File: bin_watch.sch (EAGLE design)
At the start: 88 parts, among them IC1 MEGA48/88/168-AU, J1 USB3100-XX-X_REVB, Q1 32.768kHz, T1 2N7002BKV, T2 2N7002BKV, T3 2N7002BKV, T4 2N7002BKV, T5 PMDT670UPE, T6 PMDT670UPE, T7 PMDT670UPE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

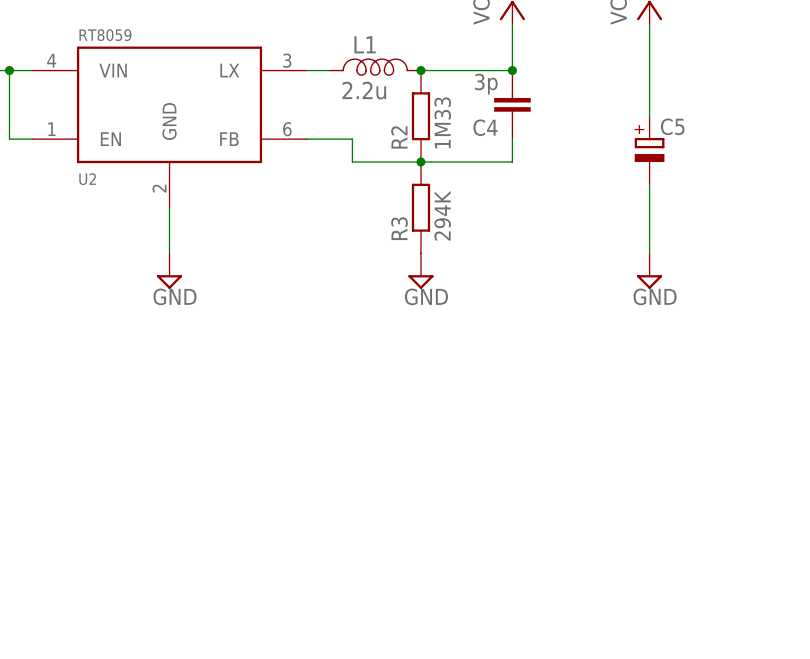
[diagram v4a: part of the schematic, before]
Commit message: Added potentiometer
This is to enable small adjustments to the system voltage around 3.5 V
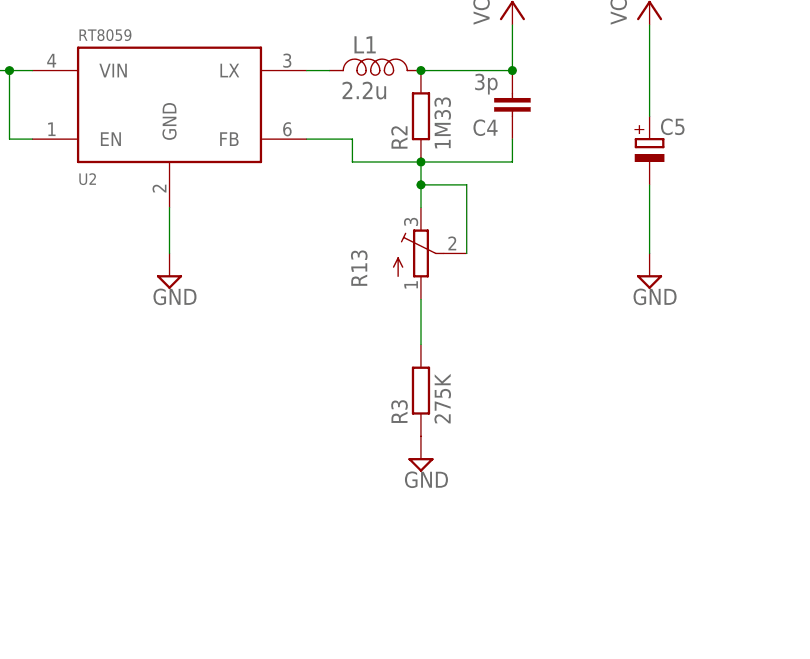
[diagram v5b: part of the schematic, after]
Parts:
- added R13: (no value), pot:TRIM_EU-3223J
- C1, C2, C3, C4: device rcl:C-EUC0805 -> rcl:C-EUC0603
- R1, R2, R4: device rcl:R-EU_R0805 -> rcl:R-EU_R0603
- R3: value 294K -> 275K; device rcl:R-EU_R0805 -> rcl:R-EU_R0603
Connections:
- new net N$10: R13.A, R3.2
- net FB: now also R13.E, R13.S; no longer R3.2
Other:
- moved on the sheet: R3
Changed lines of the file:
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@@
 <parts>
 <part name="Q1" library="crystal-geyer_V1_0" library_urn="urn:adsk.eagle:library:203" deviceset="KX-327" device="-NHF" value="32.768kHz"/>
-<part name="C1" library="rcl" library_urn="urn:adsk.eagle:library:334" deviceset="C-EU" device="C0805" package3d_urn="urn:adsk.eagle:package:23617/1" value="10pF"/>
+<part name="C1" library="rcl" library_urn="urn:adsk.eagle:library:334" deviceset="C-EU" device="C0603" package3d_urn="urn:adsk.eagle:package:23616/1" value="10pF"/>
 <part name="SUPPLY2" library="supply2" library_urn="urn:adsk.eagle:library:372" deviceset="GND" device=""/>
 <part name="JP1" library="avr-5" deviceset="AVR-ISP-6" device=""/>
@@
 <part name="SUPPLY17" library="supply2" library_urn="urn:adsk.eagle:library:372" deviceset="GND" device=""/>
 <part name="SUPPLY18" library="supply2" library_urn="urn:adsk.eagle:library:372" deviceset="GND" device=""/>
-<part name="R1" library="rcl" library_urn="urn:adsk.eagle:library:334" deviceset="R-EU_" device="R0805" package3d_urn="urn:adsk.eagle:package:23553/1" value="2K"/>
+<part name="R1" library="rcl" library_urn="urn:adsk.eagle:library:334" deviceset="R-EU_" device="R0603" package3d_urn="urn:adsk.eagle:package:23555/1" value="2K"/>
 <part name="SUPPLY19" library="supply2" library_urn="urn:adsk.eagle:library:372" deviceset="GND" device=""/>
 <part name="STAT_LED" library="standardparts" deviceset="LED" device=".0603" value="R"/>
-<part name="R4" library="rcl" library_urn="urn:adsk.eagle:library:334" deviceset="R-EU_" device="R0805" package3d_urn="urn:adsk.eagle:package:23553/1" value="470R"/>
-<part name="C3" library="rcl" library_urn="urn:adsk.eagle:library:334" deviceset="C-EU" device="C0805" package3d_urn="urn:adsk.eagle:package:23617/1" value="4.7u"/>
+<part name="R4" library="rcl" library_urn="urn:adsk.eagle:library:334" deviceset="R-EU_" device="R0603" package3d_urn="urn:adsk.eagle:package:23555/1" value="470R"/>
+<part name="C3" library="rcl" library_urn="urn:adsk.eagle:library:334" deviceset="C-EU" device="C0603" package3d_urn="urn:adsk.eagle:package:23616/1" value="4.7u"/>
 <part name="SUPPLY20" library="supply2" library_urn="urn:adsk.eagle:library:372" deviceset="GND" device=""/>
-<part name="C2" library="rcl" library_urn="urn:adsk.eagle:library:334" deviceset="C-EU" device="C0805" package3d_urn="urn:adsk.eagle:package:23617/1" value="4.7u"/>
+<part name="C2" library="rcl" library_urn="urn:adsk.eagle:library:334" deviceset="C-EU" device="C0603" package3d_urn="urn:adsk.eagle:package:23616/1" value="4.7u"/>
 <part name="SUPPLY21" library="supply2" library_urn="urn:adsk.eagle:library:372" deviceset="GND" device=""/>
 <part name="SUPPLY22" library="supply2" library_urn="urn:adsk.eagle:library:372" deviceset="GND" device=""/>
@@
 <part name="U2" library="pmg-library" deviceset="RT8059" device=""/>
 <part name="L1" library="inductor" deviceset="COIL-H" device="I" value="2.2u"/>
-<part name="R2" library="rcl" library_urn="urn:adsk.eagle:library:334" deviceset="R-EU_" device="R0805" package3d_urn="urn:adsk.eagle:package:23553/1" value="1M33"/>
-<part name="R3" library="rcl" library_urn="urn:adsk.eagle:library:334" deviceset="R-EU_" device="R0805" package3d_urn="urn:adsk.eagle:package:23553/1" value="294K"/>
-<part name="C4" library="rcl" library_urn="urn:adsk.eagle:library:334" deviceset="C-EU" device="C0805" package3d_urn="urn:adsk.eagle:package:23617/1" value="3p"/>
+<part name="R2" library="rcl" library_urn="urn:adsk.eagle:library:334" deviceset="R-EU_" device="R0603" package3d_urn="urn:adsk.eagle:package:23555/1" value="1M33"/>
+<part name="R3" library="rcl" library_urn="urn:adsk.eagle:library:334" deviceset="R-EU_" device="R0603" package3d_urn="urn:adsk.eagle:package:23555/1" value="275K"/>
+<part name="C4" library="rcl" library_urn="urn:adsk.eagle:library:334" deviceset="C-EU" device="C0603" package3d_urn="urn:adsk.eagle:package:23616/1" value="3p"/>
 <part name="SUPPLY23" library="supply2" library_urn="urn:adsk.eagle:library:372" deviceset="GND" device=""/>
 <part name="P+9" library="supply1" library_urn="urn:adsk.eagle:library:371" deviceset="VCC" device=""/>
@@
 <part name="R11" library="rcl" library_urn="urn:adsk.eagle:library:334" deviceset="R-EU_" device="R0603" package3d_urn="urn:adsk.eagle:package:23555/1" value="12"/>
 <part name="R12" library="rcl" library_urn="urn:adsk.eagle:library:334" deviceset="R-EU_" device="R0603" package3d_urn="urn:adsk.eagle:package:23555/1" value="12"/>
+<part name="R13" library="pot" library_urn="urn:adsk.eagle:library:331" deviceset="TRIM_EU-" device="3223J" package3d_urn="urn:adsk.eagle:package:22724/1"/>
 </parts>
 <sheets>
@@
 <instance part="L1" gate="G$1" x="236.22" y="246.38"/>
 <instance part="R2" gate="G$1" x="241.3" y="241.3" rot="R90"/>
-<instance part="R3" gate="G$1" x="241.3" y="231.14" rot="R90"/>
+<instance part="R3" gate="G$1" x="241.3" y="210.82" rot="R90"/>
 <instance part="C4" gate="G$1" x="251.46" y="241.3" rot="R180"/>
-<instance part="SUPPLY23" gate="GND" x="241.3" y="223.52"/>
+<instance part="SUPPLY23" gate="GND" x="241.3" y="203.2"/>
 <instance part="P+9" gate="VCC" x="266.7" y="254"/>
 <instance part="C5" gate="G$1" x="266.7" y="238.76"/>
@@
 <instance part="R11" gate="G$1" x="266.7" y="55.88"/>
 <instance part="R12" gate="G$1" x="274.32" y="53.34"/>
+<instance part="R13" gate="1" x="241.3" y="226.06"/>
 </instances>
 <busses>
@@
 <net name="FB" class="0">
 <segment>
-<pinref part="R2" gate="G$1" pin="1"/>
-<pinref part="R3" gate="G$1" pin="2"/>
 <pinref part="U2" gate="G$1" pin="FB"/>
 <wire x1="228.6" y1="238.76" x2="233.68" y2="238.76" width="0.1524" layer="91"/>
 <wire x1="233.68" y1="238.76" x2="233.68" y2="236.22" width="0.1524" layer="91"/>
+<pinref part="R2" gate="G$1" pin="1"/>
+<pinref part="R13" gate="1" pin="E"/>
+<wire x1="241.3" y1="231.14" x2="241.3" y2="233.68" width="0.1524" layer="91"/>
+<wire x1="241.3" y1="233.68" x2="241.3" y2="236.22" width="0.1524" layer="91"/>
 <wire x1="233.68" y1="236.22" x2="241.3" y2="236.22" width="0.1524" layer="91"/>
 <junction x="241.3" y="236.22"/>
 <pinref part="C4" gate="G$1" pin="1"/>
+<wire x1="251.46" y1="236.22" x2="251.46" y2="238.76" width="0.1524" layer="91"/>
 <wire x1="241.3" y1="236.22" x2="251.46" y2="236.22" width="0.1524" layer="91"/>
-<wire x1="251.46" y1="236.22" x2="251.46" y2="238.76" width="0.1524" layer="91"/>
+<pinref part="R13" gate="1" pin="S"/>
+<wire x1="246.38" y1="226.06" x2="246.38" y2="233.68" width="0.1524" layer="91"/>
+<wire x1="246.38" y1="233.68" x2="241.3" y2="233.68" width="0.1524" layer="91"/>
+<junction x="241.3" y="233.68"/>
 </segment>
 </net>
@@
 </segment>
 </net>
+<net name="N$10" class="0">
+<segment>
+<pinref part="R3" gate="G$1" pin="2"/>
+<pinref part="R13" gate="1" pin="A"/>
+<wire x1="241.3" y1="220.98" x2="241.3" y2="215.9" width="0.1524" layer="91"/>
+</segment>
+</net>

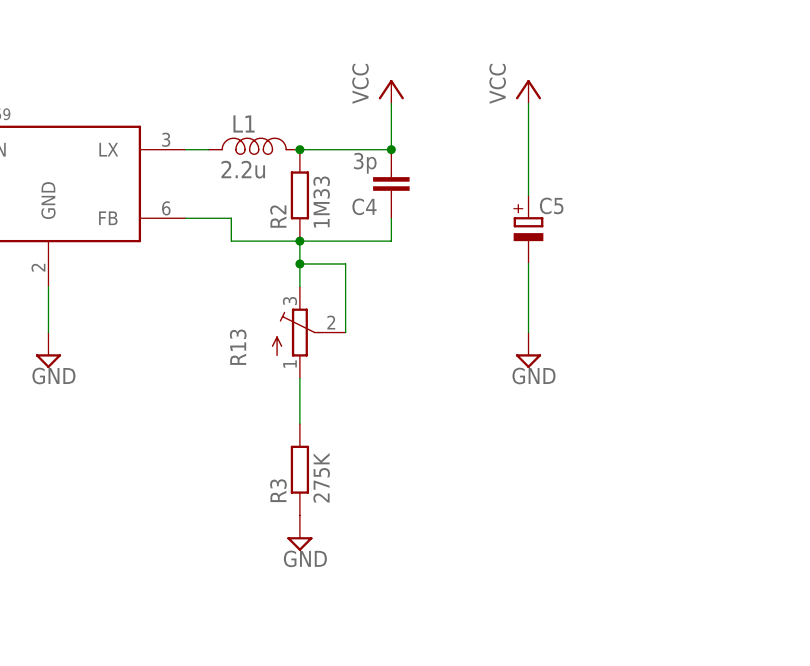
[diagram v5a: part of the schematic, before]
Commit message: Little tweaks
Ipdated component names, positions, and version label.
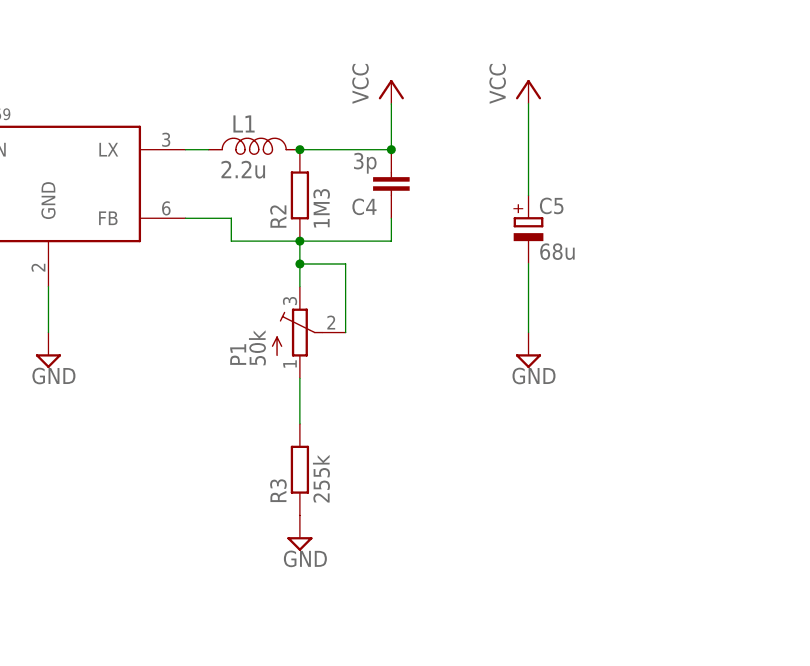
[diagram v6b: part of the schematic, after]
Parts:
- C5: value (none) -> 68u
- P1: value (none) -> 50k
- R2: value 1M33 -> 1M3
- R3: value 275K -> 255k
- renumbered R13 to P1
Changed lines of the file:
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@@
 <part name="U2" library="pmg-library" deviceset="RT8059" device=""/>
 <part name="L1" library="inductor" deviceset="COIL-H" device="I" value="2.2u"/>
-<part name="R2" library="rcl" library_urn="urn:adsk.eagle:library:334" deviceset="R-EU_" device="R0603" package3d_urn="urn:adsk.eagle:package:23555/1" value="1M33"/>
-<part name="R3" library="rcl" library_urn="urn:adsk.eagle:library:334" deviceset="R-EU_" device="R0603" package3d_urn="urn:adsk.eagle:package:23555/1" value="275K"/>
+<part name="R2" library="rcl" library_urn="urn:adsk.eagle:library:334" deviceset="R-EU_" device="R0603" package3d_urn="urn:adsk.eagle:package:23555/1" value="1M3"/>
+<part name="R3" library="rcl" library_urn="urn:adsk.eagle:library:334" deviceset="R-EU_" device="R0603" package3d_urn="urn:adsk.eagle:package:23555/1" value="255k"/>
 <part name="C4" library="rcl" library_urn="urn:adsk.eagle:library:334" deviceset="C-EU" device="C0603" package3d_urn="urn:adsk.eagle:package:23616/1" value="3p"/>
 <part name="SUPPLY23" library="supply2" library_urn="urn:adsk.eagle:library:372" deviceset="GND" device=""/>
 <part name="P+9" library="supply1" library_urn="urn:adsk.eagle:library:371" deviceset="VCC" device=""/>
-<part name="C5" library="rcl" library_urn="urn:adsk.eagle:library:334" deviceset="CPOL-EU" device="B/3528-21R" package3d_urn="urn:adsk.eagle:package:23409/1"/>
+<part name="C5" library="rcl" library_urn="urn:adsk.eagle:library:334" deviceset="CPOL-EU" device="B/3528-21R" package3d_urn="urn:adsk.eagle:package:23409/1" value="68u"/>
 <part name="R5" library="rcl" library_urn="urn:adsk.eagle:library:334" deviceset="R-EU_" device="R0603" package3d_urn="urn:adsk.eagle:package:23555/1" value="12"/>
 <part name="R6" library="rcl" library_urn="urn:adsk.eagle:library:334" deviceset="R-EU_" device="R0603" package3d_urn="urn:adsk.eagle:package:23555/1" value="12"/>
@@
 <part name="R11" library="rcl" library_urn="urn:adsk.eagle:library:334" deviceset="R-EU_" device="R0603" package3d_urn="urn:adsk.eagle:package:23555/1" value="12"/>
 <part name="R12" library="rcl" library_urn="urn:adsk.eagle:library:334" deviceset="R-EU_" device="R0603" package3d_urn="urn:adsk.eagle:package:23555/1" value="12"/>
-<part name="R13" library="pot" library_urn="urn:adsk.eagle:library:331" deviceset="TRIM_EU-" device="3223J" package3d_urn="urn:adsk.eagle:package:22724/1"/>
+<part name="P1" library="pot" library_urn="urn:adsk.eagle:library:331" deviceset="TRIM_EU-" device="3223J" package3d_urn="urn:adsk.eagle:package:22724/1" value="50k"/>
 </parts>
 <sheets>
@@
 <instance part="R11" gate="G$1" x="266.7" y="55.88"/>
 <instance part="R12" gate="G$1" x="274.32" y="53.34"/>
-<instance part="R13" gate="1" x="241.3" y="226.06"/>
+<instance part="P1" gate="1" x="241.3" y="226.06"/>
 </instances>
 <busses>
@@
 <wire x1="233.68" y1="238.76" x2="233.68" y2="236.22" width="0.1524" layer="91"/>
 <pinref part="R2" gate="G$1" pin="1"/>
-<pinref part="R13" gate="1" pin="E"/>
+<pinref part="P1" gate="1" pin="E"/>
 <wire x1="241.3" y1="231.14" x2="241.3" y2="233.68" width="0.1524" layer="91"/>
 <wire x1="241.3" y1="233.68" x2="241.3" y2="236.22" width="0.1524" layer="91"/>
@@
 <wire x1="251.46" y1="236.22" x2="251.46" y2="238.76" width="0.1524" layer="91"/>
 <wire x1="241.3" y1="236.22" x2="251.46" y2="236.22" width="0.1524" layer="91"/>
-<pinref part="R13" gate="1" pin="S"/>
+<pinref part="P1" gate="1" pin="S"/>
 <wire x1="246.38" y1="226.06" x2="246.38" y2="233.68" width="0.1524" layer="91"/>
 <wire x1="246.38" y1="233.68" x2="241.3" y2="233.68" width="0.1524" layer="91"/>
@@
 <segment>
 <pinref part="R3" gate="G$1" pin="2"/>
-<pinref part="R13" gate="1" pin="A"/>
+<pinref part="P1" gate="1" pin="A"/>
 <wire x1="241.3" y1="220.98" x2="241.3" y2="215.9" width="0.1524" layer="91"/>
 </segment>

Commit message: Added fiducial marks
Some minor adjustments to the traces, and added fiducial marks for the board and for the chip.
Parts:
- added U$1, U$2, U$3: FIDUCIAL, adafruit:FIDUCIAL
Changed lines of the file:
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@@
 <?xml version="1.0" encoding="utf-8"?>
 <!DOCTYPE eagle SYSTEM "eagle.dtd">
-<eagle version="8.3.0">
+<eagle version="8.3.1">
 <drawing>
 <settings>
@@
 <part name="R12" library="rcl" library_urn="urn:adsk.eagle:library:334" deviceset="R-EU_" device="R0603" package3d_urn="urn:adsk.eagle:package:23555/1" value="12"/>
 <part name="P1" library="pot" library_urn="urn:adsk.eagle:library:331" deviceset="TRIM_EU-" device="3223J" package3d_urn="urn:adsk.eagle:package:22724/1" value="50k"/>
+<part name="U$1" library="adafruit" library_urn="urn:adsk.eagle:library:420" deviceset="FIDUCIAL" device=""/>
+<part name="U$2" library="adafruit" library_urn="urn:adsk.eagle:library:420" deviceset="FIDUCIAL" device=""/>
+<part name="U$3" library="adafruit" library_urn="urn:adsk.eagle:library:420" deviceset="FIDUCIAL" device=""/>
 </parts>
 <sheets>
@@
 <instance part="R12" gate="G$1" x="274.32" y="53.34"/>
 <instance part="P1" gate="1" x="241.3" y="226.06"/>
+<instance part="U$1" gate="G$1" x="88.9" y="-53.34"/>
+<instance part="U$2" gate="G$1" x="88.9" y="-63.5"/>
+<instance part="U$3" gate="G$1" x="88.9" y="-73.66"/>
 </instances>
 <busses>

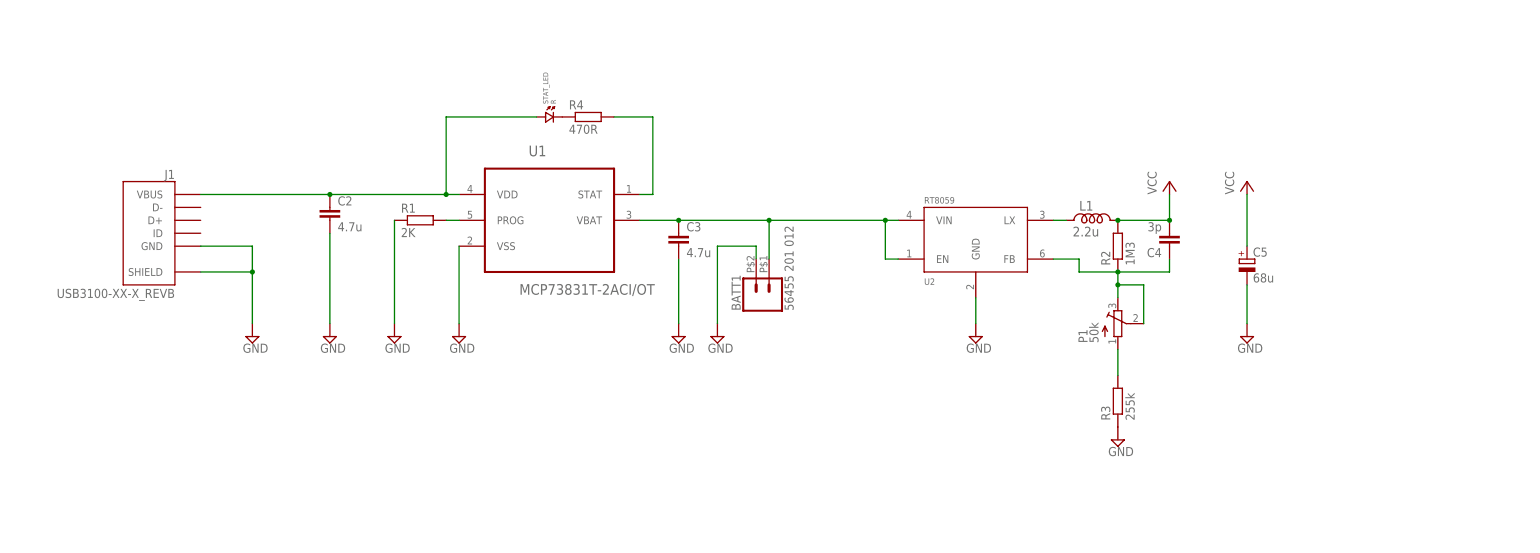
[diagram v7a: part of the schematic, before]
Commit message: Changed power supply to 5V
Replaced the Buck converter with a Boost converter. Saved some space.
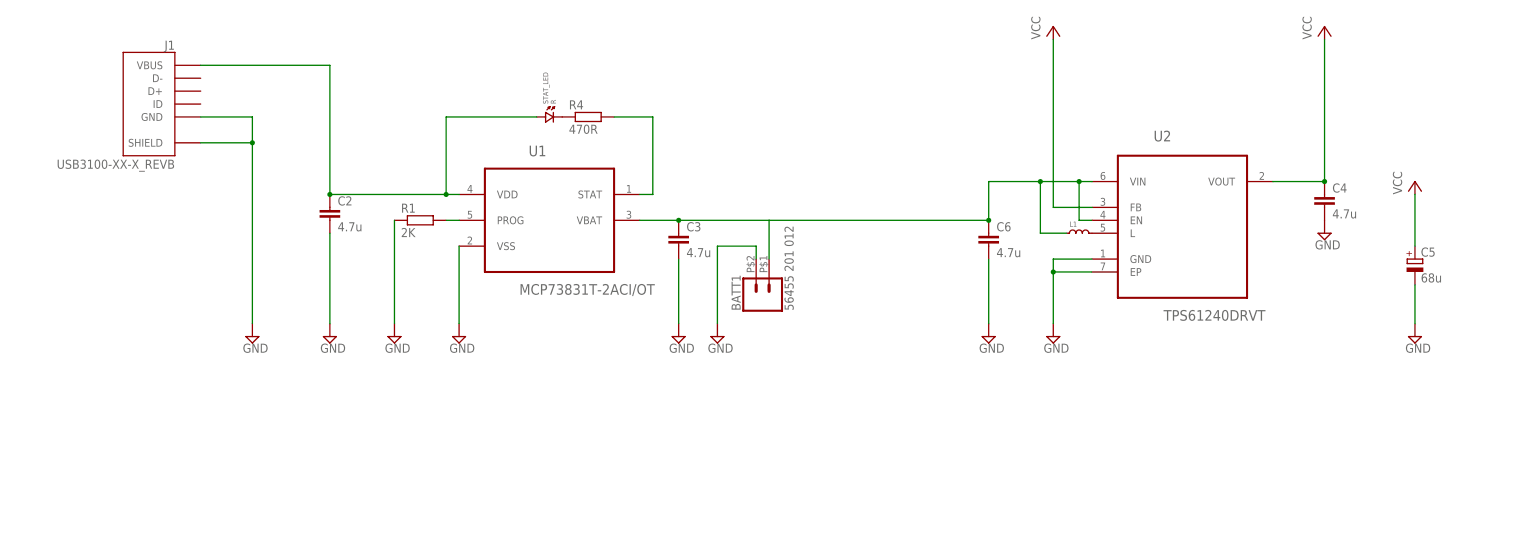
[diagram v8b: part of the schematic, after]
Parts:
- removed P1: 50k, pot:TRIM_EU-3223J
- removed R2: 1M3, rcl:R-EU_R0603
- removed R3: 255k, rcl:R-EU_R0603
- added C6: 4.7u, rcl:C-EUC0603
- C4: value 3p -> 4.7u
- L1: value 2.2u -> (none); device inductor:COIL-HI -> standardparts:RF-INDUCTOR.0805
- U2: value RT8059 -> TPS61240DRVT; device pmg-library:RT8059 -> Texas Instruments_By_element14_Batch_1:TPS61240DRVT
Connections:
- removed net FB: C4.1, P1.E, P1.S, R2.1, U2.FB
- removed net LX: L1.L, U2.LX
- removed net N$10: P1.A, R3.2
- new net L: L1.2, U2.L
- net GND: now also C4.2, C6.2, U2.EP; no longer R3.1
- net VBATT: now also C6.1, L1.1
- net VCC: now also C4.1, U2.FB, U2.VOUT; no longer C4.2, L1.R, R2.2
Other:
- moved on the sheet: C4, C5, J1
